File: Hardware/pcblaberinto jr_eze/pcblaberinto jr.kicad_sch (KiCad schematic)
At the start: 19 parts, among them J1 Ultrasonido, J2 Ultrasonido, J3 Ultrasonido, J4 CableAlimentacion, J5 Jumper, J7 EncoderMotorDerecha, J8 EncoderMotorIzquierda, J9 Input of Driver L9110, SW1 SW_Push, U1 L7805

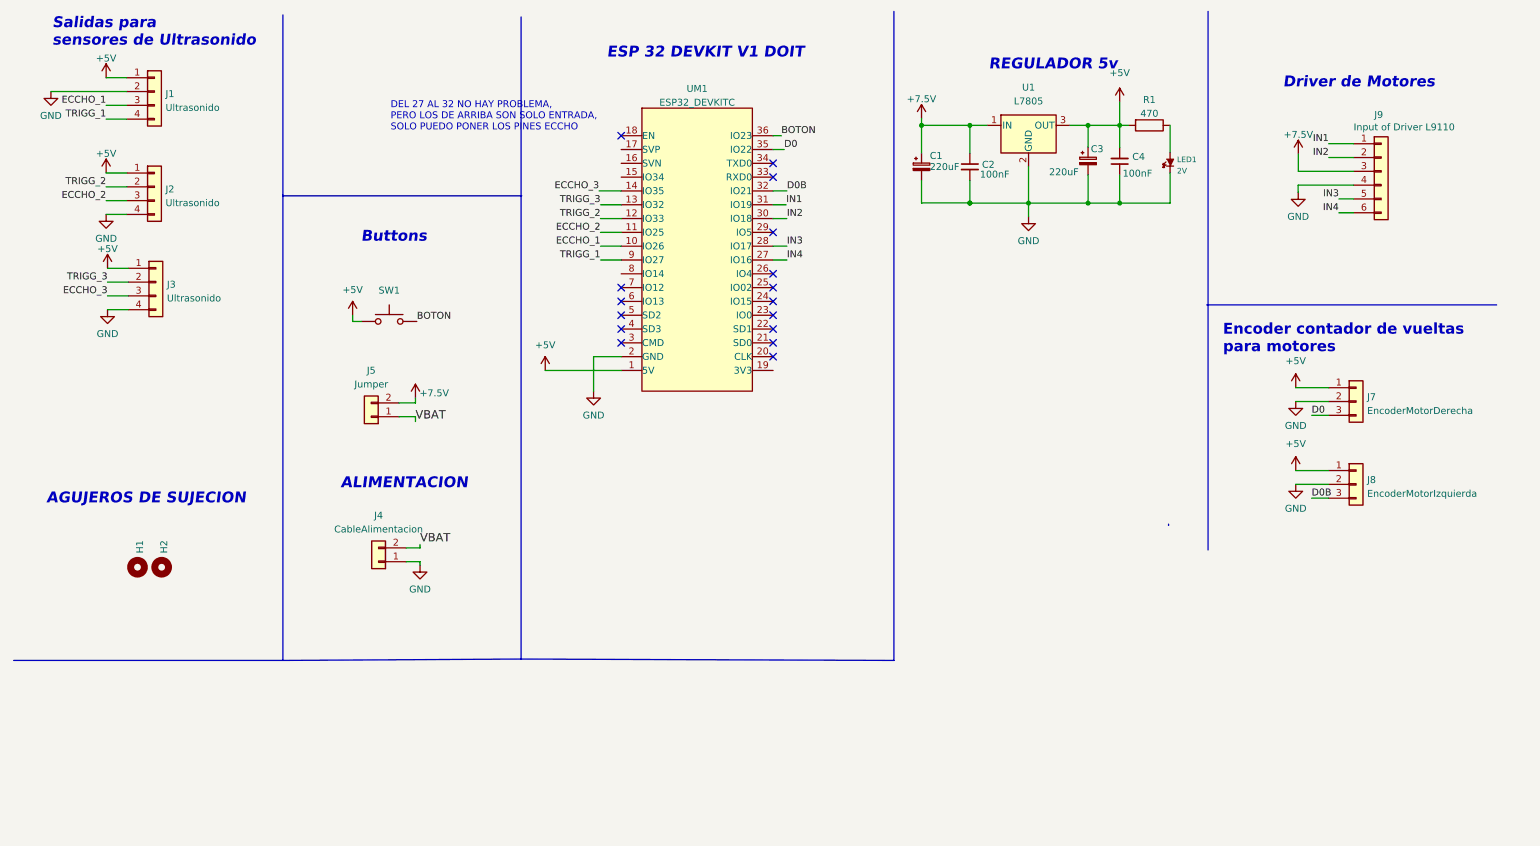
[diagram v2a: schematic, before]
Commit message: agregando la placa de bover ORIGIN Y ORDENANDO UN POCO
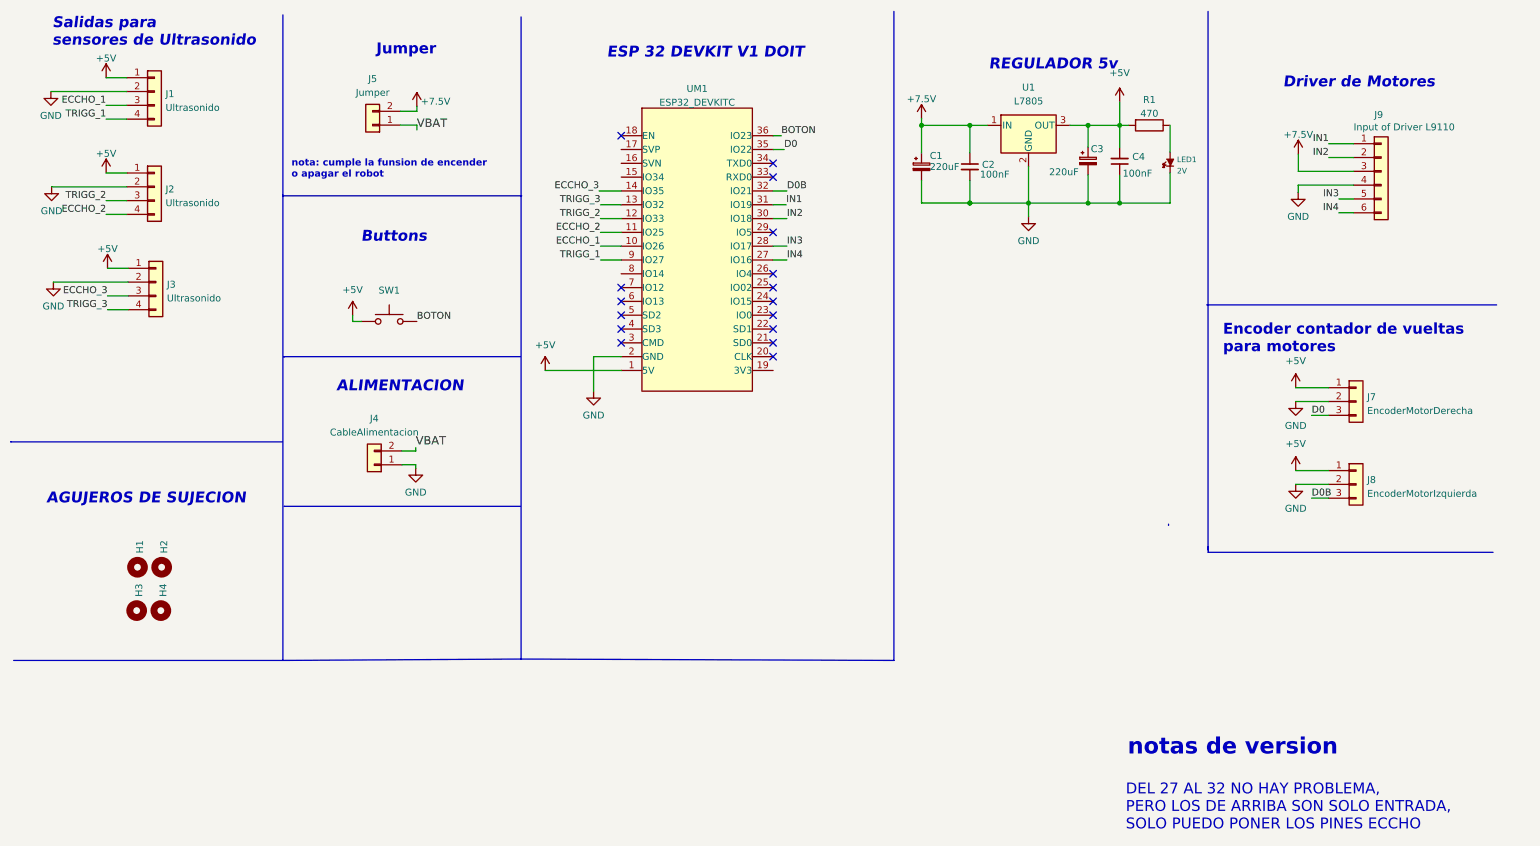
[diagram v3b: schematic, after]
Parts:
- added H3, H4: Mounting_Hole, EESTN5:hole_3mm, symbol EESTN5:Mounting_Hole
- C1, C3: footprint (none) -> EESTN5:CAP_ELEC_5x11mm
- H1, H2: footprint EESTN5:pad_2mm -> EESTN5:hole_3mm
- J1, J2, J3: footprint EESTN5:pin_strip_4 -> Connector_JST:JST_EH_B4B-EH-A_1x04_P2.50mm_Vertical
- J4: footprint Connector_PinHeader_2.54mm:PinHeader_1x02_P2.54mm_Vertical -> Connector_JST:JST_EH_B2B-EH-A_1x02_P2.50mm_Vertical
- J5: footprint EESTN522:Jumper -> EESTN5:Jumper
- J7, J8: footprint EESTN5:Pin_Strip_3 -> Connector_JST:JST_EH_B3B-EH-A_1x03_P2.50mm_Vertical
- J9: footprint EESTN5:Pin_Header_6 -> Connector_JST:JST_EH_B6B-EH-A_1x06_P2.50mm_Vertical
- LED1: footprint (none) -> EESTN5:led_3mm_red
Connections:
- net ECCHO_2: now also J2.4 (Pin_4); no longer J2.3 (Pin_3)
- net GND: now also J2.2 (Pin_2), J3.2 (Pin_2); no longer J2.4 (Pin_4), J3.4 (Pin_4)
- net TRIGG_2: now also J2.3 (Pin_3); no longer J2.2 (Pin_2)
- net TRIGG_3: now also J3.4 (Pin_4); no longer J3.2 (Pin_2)
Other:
- note added: "Jumper"
- note added: "nota: cumple la funsion de encender o apagar el robot"
- note added: "notas de version"
- moved on the sheet: J4, J5
